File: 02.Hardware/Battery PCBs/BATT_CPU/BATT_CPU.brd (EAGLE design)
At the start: 30.5 x 23.5 mm, 68 parts, among them J1 2314820-6, K3 FLEX_CONN, K4 FLEX6, K5 FLEX8, U1 ATSAMD21G18_QFN, U2 TPS78230DDCR, U3 TPS78230DDCR, U4 TS3USB221A, U5 MAX9062EUK+T, U6 MAX9062EUK+T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

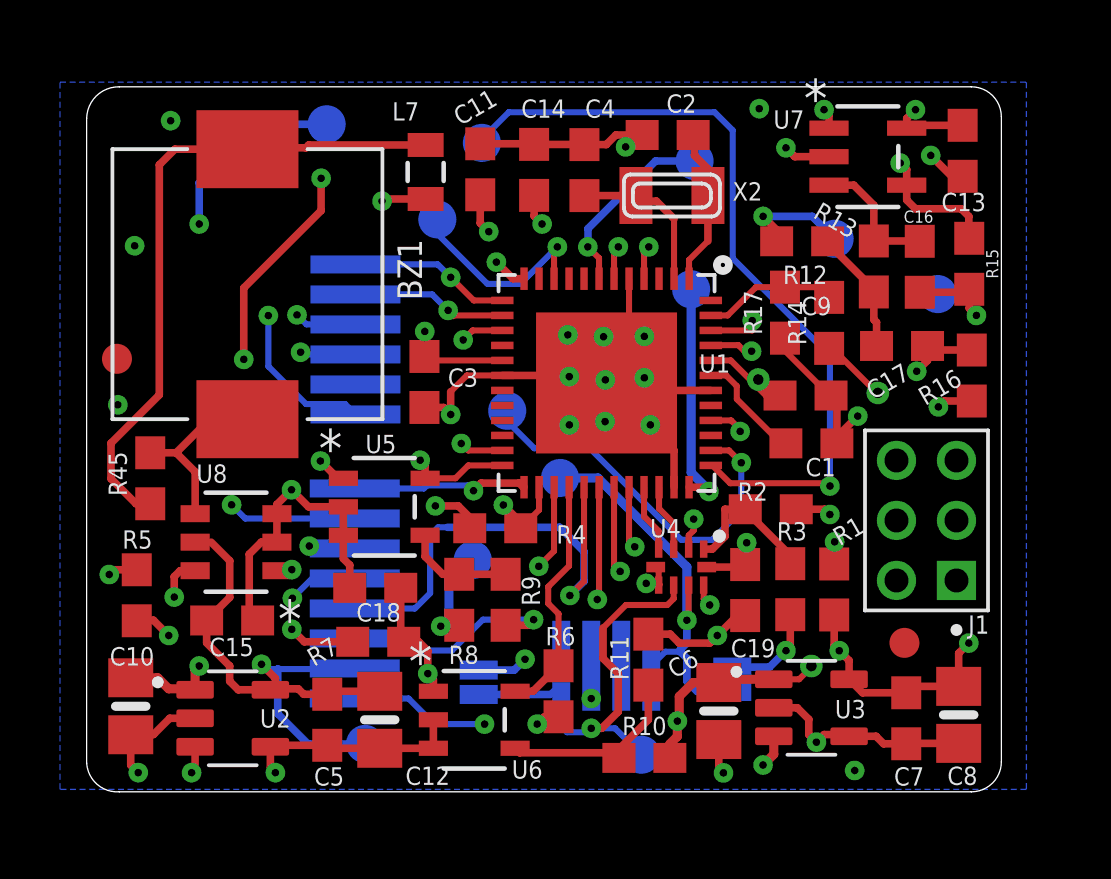
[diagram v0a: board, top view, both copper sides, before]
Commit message: Cambios revisados con David
Revision de los pcbs de la bateria.

En el DCDC se añade un diode Clamp (bat54s) en la medicion de la tension de salida.
Actualizacion de la BOM a v8.
Documentos de Cambios de versiones
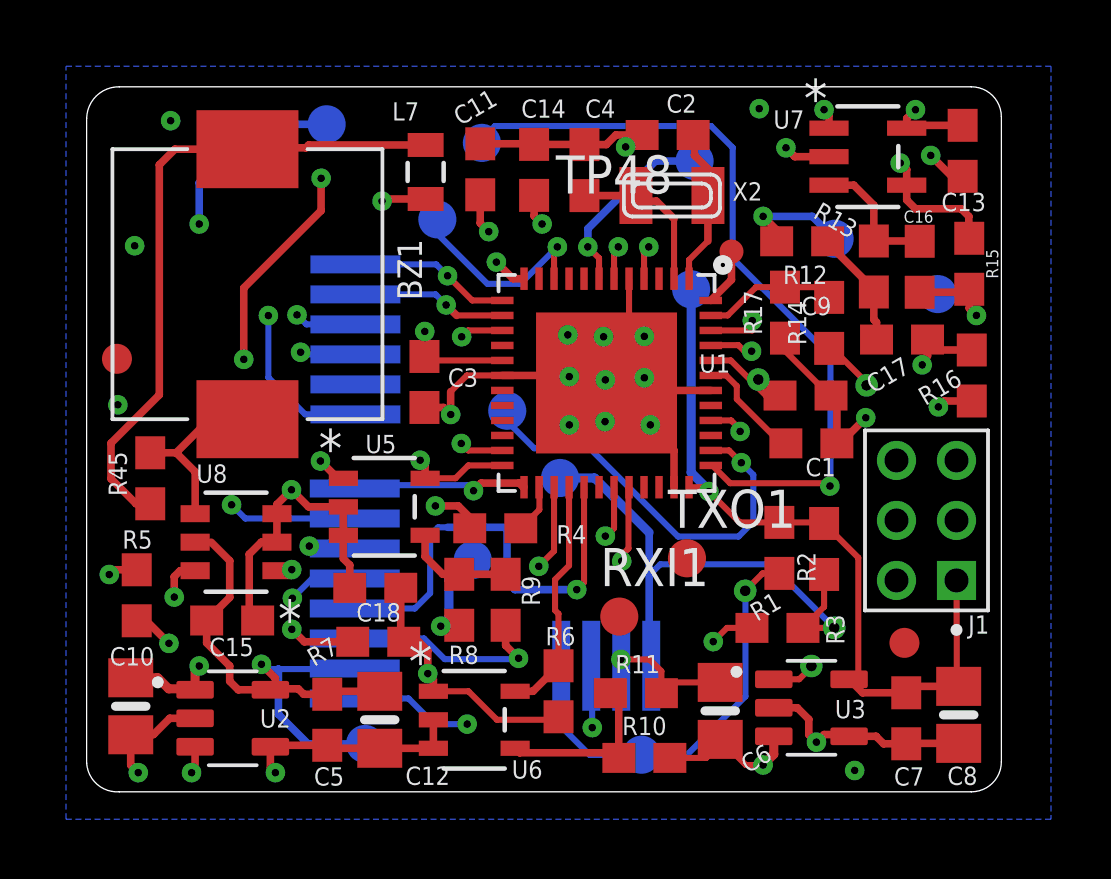
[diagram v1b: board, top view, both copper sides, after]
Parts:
- removed C19: 100n, microbuilder:0603-NO
- removed JP1, JP2: JUMPER-SMT_2_NO_SILK, SparkFun-Jumpers:SMT-JUMPER_2_NO_SILK
- removed U4: TS3USB221A, SparkFun-IC-Special-Function:QFN-10-RSE
- added RXI1, TXO1: TESTPAD_TPSQB1,27, BeagleBone_Blue_R3:TESTPAD_B1,27
- added TP48: TPTP08R, testpad:TP08R
- moved R1 2.29 mm to (47.2, 14.8), turned to 90 degrees
- moved R2 2.22 mm to (48.6, 14.7), turned to 90 degrees
- moved R3 1.36 mm to (47.1, 12.1), turned to 180 degrees
- moved R11 1.19 mm to (42.4, 9.93), turned to 0 degrees
- moved C17 0.21 mm to (51.2, 21.7)
- turned C6 to 90 degrees
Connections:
- removed net N$2: R2.1, R3.1, U4.1
- removed net N$3: R1.1, R4.1, U4.2
- net D+: no longer U4.3
- net D-: no longer U4.4
- net GND: no longer C19.2, U4.5, U4.6
- net N$15: now also TP48.TP
- net RXI: now also RXI1.TP
- net SCL2_CPU: no longer JP2.1
- net SCL_2: now also R1.1, R4.1; no longer JP2.2, U4.7
- net SDA2_CPU: no longer JP1.1
- net SDA_2: now also R2.1, R3.1; no longer JP1.2, U4.8
- net TXO: now also TXO1.TP
- net USB_SEL: no longer U4.9
- net VCC: no longer C19.1, U4.10
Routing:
- net N$3: track 17.8 -> 0.00 mm, vias 3 -> 0
- net SCL_2: track 16.0 -> 28.9 mm, vias 1 -> 2
- net VCC: track 37.0 -> 45.6 mm, vias 12 -> 7
- net USB_SEL: track 8.55 -> 0.00 mm, vias 2 -> 0
- net SCL2_CPU: track 9.87 -> 1.63 mm, vias 2 -> 0
- net SDA_2: track 13.5 -> 21.5 mm
- net VBUS: track 58.8 -> 64.1 mm, vias 7 -> 6
- net N$2: track 4.90 -> 0.00 mm
- net SDA2_CPU: track 16.5 -> 11.7 mm
- net SWCLK: track 12.3 -> 9.45 mm
- net D+: track 2.27 -> 0.00 mm
- net D-: track 2.27 -> 0.00 mm
- net N$15: track 0.00 -> 1.92 mm
- net GND: track 79.4 -> 77.5 mm, vias 29 -> 27
- net SDA: track 32.1 -> 30.5 mm
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
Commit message: Revision antes de Produccion
r6, r7: 120k a 10k
r45: no se monta
se añaden notas
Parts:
- R6, R7: value 120k -> 10k
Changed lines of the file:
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@@
 <drawing>
 <settings>
-<setting alwaysvectorfont="yes"/>
+<setting alwaysvectorfont="no"/>
 <setting keepoldvectorfont="yes"/>
 <setting verticaltext="up"/>
@@
 <attribute name="VENDOR" value="Maxim Integrated Products" x="36.98" y="9.04" size="1.778" layer="27" display="off"/>
 </element>
-<element name="R6" library="SparkFun-Resistors" package="0603" value="120k" x="39.79" y="9.99" smashed="yes" rot="R270">
+<element name="R6" library="SparkFun-Resistors" package="0603" value="10k" x="39.79" y="9.99" smashed="yes" rot="R270">
 <attribute name="NAME" x="39.854" y="11.522" size="0.6096" layer="25" font="vector" align="bottom-center"/>
 <attribute name="PROD_ID" value=" " x="39.79" y="9.99" size="1.778" layer="27" rot="R270" display="off"/>
 <attribute name="VALUE" x="39.208" y="10.09" size="0.4064" layer="27" font="vector" rot="R270" align="top-center"/>
 </element>
-<element name="R7" library="SparkFun-Resistors" package="0603" value="120k" x="33.78" y="11.64" smashed="yes">
+<element name="R7" library="SparkFun-Resistors" package="0603" value="10k" x="33.78" y="11.64" smashed="yes">
 <attribute name="NAME" x="32.071684375" y="11.050209375" size="0.6096" layer="25" font="vector" rot="R30" align="bottom-center"/>
 <attribute name="PROD_ID" value=" " x="33.78" y="11.64" size="1.778" layer="27" display="off"/>
